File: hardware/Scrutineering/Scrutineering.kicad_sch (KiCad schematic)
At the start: 17 parts, among them J1 Conn_01x04, J10 Conn_01x03, J11 Conn_01x02, J12 Conn_01x01, J13 Conn_01x01, J2 Conn_01x04, J3 Conn_01x01, J4 Conn_01x01, J5 Conn_01x03, J6 Conn_01x04, J7 Conn_01x04, J8 Conn_01x01, J9 Conn_01x01, SW1 SW_SPDT_TEMP1, SW2 SW_SPDT_TEMP2, SW3 SW_SPDT_VOLT1, SW4 SW_SPDT_VOLT2

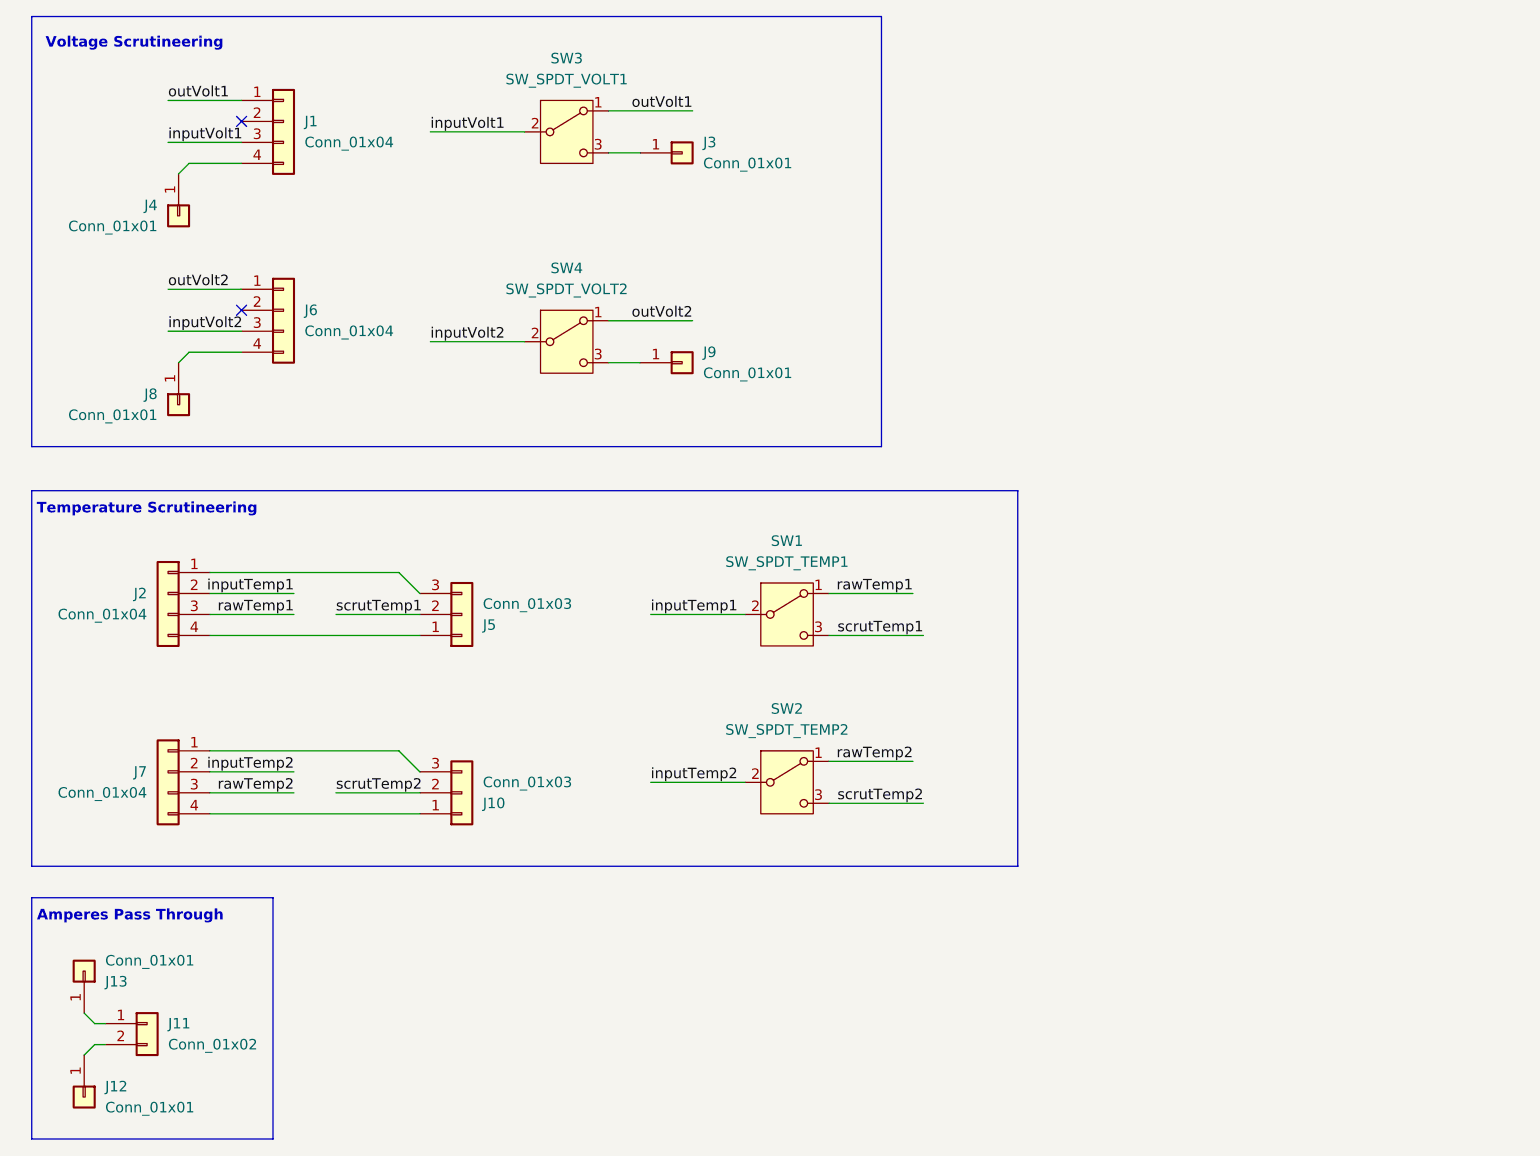
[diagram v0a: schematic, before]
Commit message: schematic with graphics/mounting
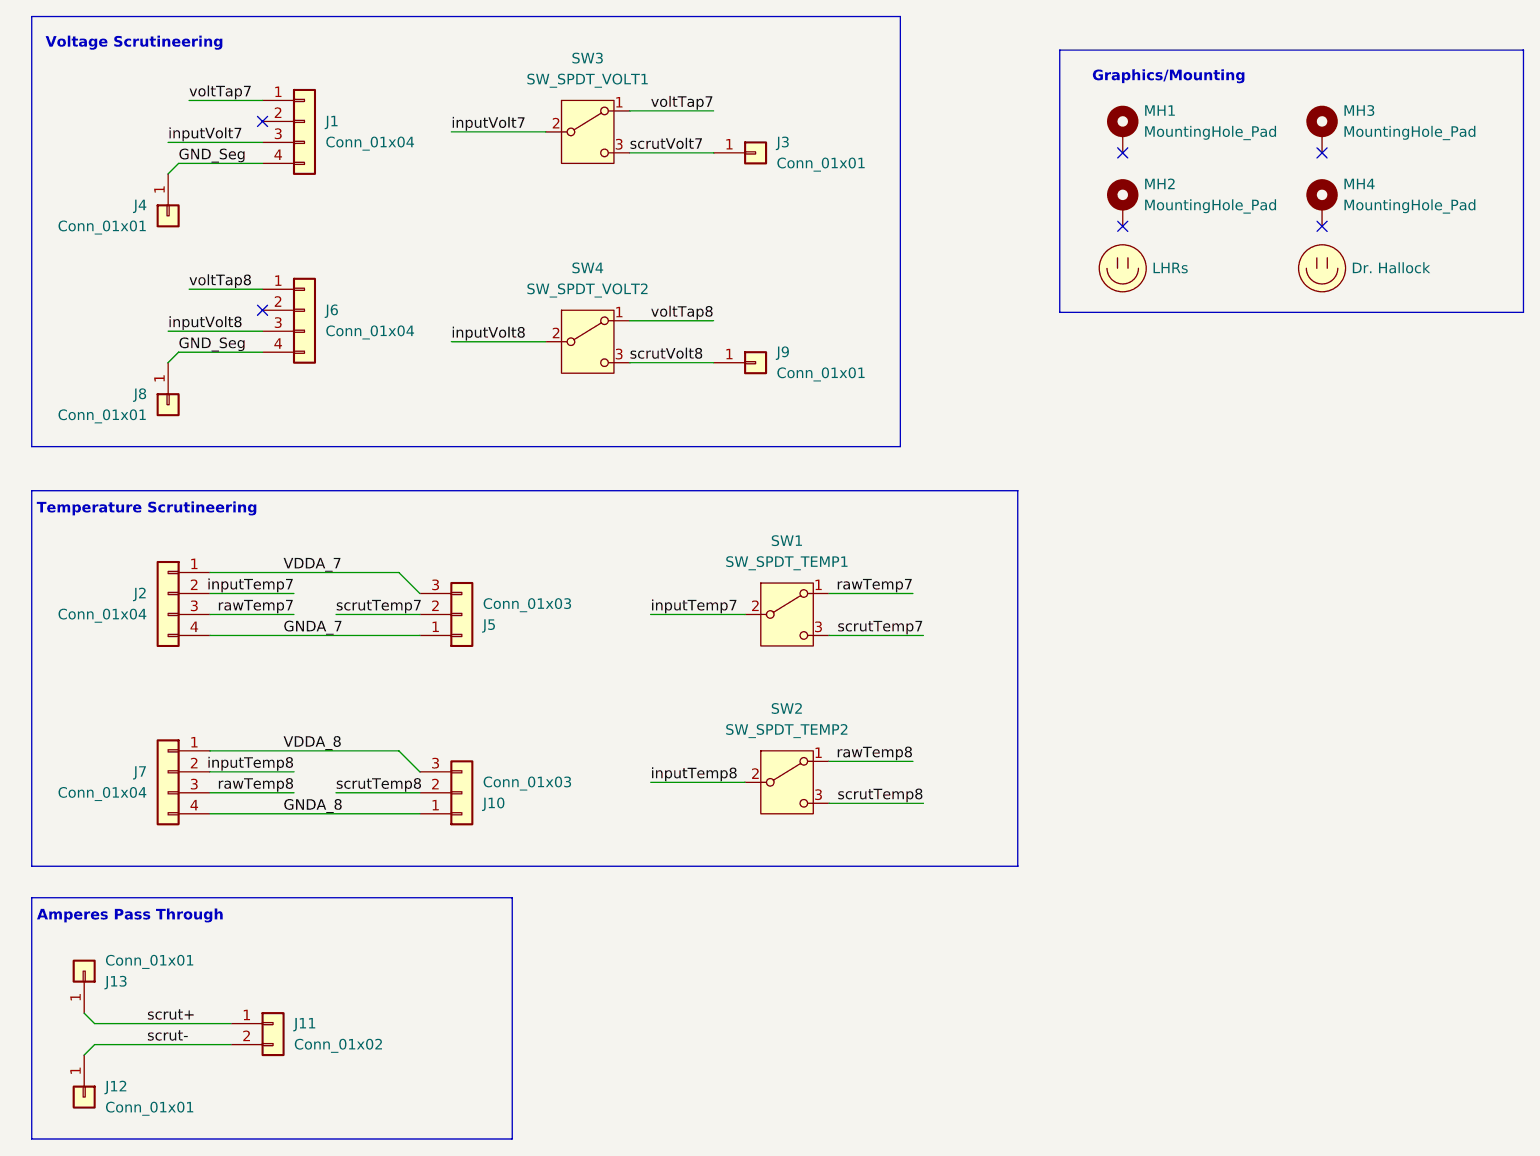
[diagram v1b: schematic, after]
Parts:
- added LOGO1: Dr. Hallock, UTSVT_Logos:Hallock_Image_Small, symbol utsvt_misc:Logo_Placeholder
- added LOGO2: LHRs, UTSVT_Logos:LHRs_LOGO, symbol utsvt_misc:Logo_Placeholder
- added MH1, MH2, MH3, MH4: MountingHole_Pad, MountingHole:MountingHole_3.2mm_M3_Pad_TopBottom, symbol Mechanical:MountingHole_Pad
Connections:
- net GND_Seg: now reaches J1.4 (Pin_4), J4.1 (Pin_1)
- net GND_Seg: now also J6.4 (Pin_4), J8.1 (Pin_1)
- net scrut+: now reaches J11.1 (Pin_1), J13.1 (Pin_1)
- net scrut-: now reaches J11.2 (Pin_2), J12.1 (Pin_1)
- net scrutVolt7: now reaches J3.1 (Pin_1), SW3.3 (C)
- net GNDA_7: now reaches J2.4 (Pin_4), J5.1 (Pin_1)
- net VDDA_7: now reaches J2.1 (Pin_1), J5.3 (Pin_3)
- net GNDA_8: now reaches J10.1 (Pin_1), J7.4 (Pin_4)
- net VDDA_8: now reaches J10.3 (Pin_3), J7.1 (Pin_1)
- net scrutVolt8: now reaches J9.1 (Pin_1), SW4.3 (C)
- net inputTemp1 renamed inputTemp7
- net inputTemp2 renamed inputTemp8
- net inputVolt1 renamed inputVolt7
- net inputVolt2 renamed inputVolt8
- net outVolt1 renamed voltTap7
- net outVolt2 renamed voltTap8
- net rawTemp1 renamed rawTemp7
- net rawTemp2 renamed rawTemp8
- net scrutTemp1 renamed scrutTemp7
- net scrutTemp2 renamed scrutTemp8
- no-connect marks 2 -> 6
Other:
- note added: "Graphics/Mounting"
- moved on the sheet: J1, J11, J3, J4, J6, J8, J9, SW3, SW4

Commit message: graphics stuff
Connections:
- net GND_Seg renamed GND_Seg7
- net GND_Seg7: no longer J6.4 (Pin_4), J8.1 (Pin_1)
- new net GND_Seg8: J6.4 (Pin_4), J8.1 (Pin_1)
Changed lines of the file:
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@@
 		)
 	)
-	(label "GND_Seg"
+	(label "GND_Seg7"
 		(at 44.45 45.72 0)
 		(effects
@@
 		)
 	)
-	(label "GND_Seg"
+	(label "GND_Seg8"
 		(at 44.45 68.58 0)
 		(effects

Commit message: BOM and gerber (still need to find jack P/N)
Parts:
- added J14: Conn_01x02, UTSVT_Connectors:105313-2102, symbol Connector_Generic:Conn_01x02
- renumbered J12 to J10, J5 to J11, J10 to J12, J11 to J13, J6 to J2, J2 to J3, J7 to J4, J4 to J5, J8 to J6, J3 to J7, J9 to J8, J13 to J9, SW3 to SW1, SW4 to SW2, SW1 to SW3, SW2 to SW4
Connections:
- net GNDA_7: now also J11.3 (Pin_3), J3.1 (Pin_1); no longer J11.1 (Pin_1), J3.4 (Pin_4)
- net GNDA_8: now also J12.3 (Pin_3), J4.1 (Pin_1); no longer J12.1 (Pin_1), J4.4 (Pin_4)
- net GND_Seg7: now also J1.1 (Pin_1); no longer J1.4 (Pin_4)
- net GND_Seg8: now also J2.1 (Pin_1); no longer J2.4 (Pin_4)
- net VDDA_7: now also J11.1 (Pin_1), J3.4 (Pin_4); no longer J11.3 (Pin_3), J3.1 (Pin_1)
- net VDDA_8: now also J12.1 (Pin_1), J4.4 (Pin_4); no longer J12.3 (Pin_3), J4.1 (Pin_1)
- net inputVolt7: now also J1.2 (Pin_2); no longer J1.3 (Pin_3)
- net inputVolt8: now also J2.2 (Pin_2); no longer J2.3 (Pin_3)
- net scrut+: now also J14.2 (Pin_2)
- net scrut-: now also J14.1 (Pin_1)
- net voltTap7: now also J1.4 (Pin_4); no longer J1.1 (Pin_1)
- net voltTap8: now also J2.4 (Pin_4); no longer J2.1 (Pin_1)
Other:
- moved on the sheet: J1, J2, J3, J4, J5, J6

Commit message: final
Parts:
- J10, J5, J6, J7, J8, J9: P/N (none) -> 105-2210-201
- TEMP1: renamed from SW3; value SW_SPDT_TEMP1 -> SW_SPDT; P/N (none) -> OS102011MS2Q
- TEMP2: renamed from SW4; value SW_SPDT_TEMP2 -> SW_SPDT; P/N (none) -> OS102011MS2Q
- VOLT1: renamed from SW1; value SW_SPDT_VOLT1 -> SW_SPDT; P/N (none) -> OS102011MS2Q
- VOLT2: renamed from SW2; value SW_SPDT_VOLT2 -> SW_SPDT; P/N (none) -> OS102011MS2Q
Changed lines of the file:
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@@
+			)
+		)
+		(property "P/N" "105-2210-201"
+			(at 114.3 44.45 0)
+			(effects
+				(font
+					(size 1.27 1.27)
+				)
+				(hide yes)
 			)
 		)
@@
 			)
 		)
+		(property "P/N" "105-2210-201"
+			(at 33.02 158.75 90)
+			(effects
+				(font
+					(size 1.27 1.27)
+				)
+				(hide yes)
+			)
+		)
 		(pin "1"
 		)
@@
 			)
 		)
+		(property "P/N" "105-2210-201"
+			(at 59.69 52.07 90)
+			(effects
+				(font
+					(size 1.27 1.27)
+				)
+				(hide yes)
+			)
+		)
 		(pin "1"
 		)
@@
 		(dnp no)
 		(fields_autoplaced yes)
-		(property "Reference" "SW1"
+		(property "Reference" "VOLT1"
 			(at 93.98 33.02 0)
 			(effects
@@
 			)
 		)
-		(property "Value" "SW_SPDT_VOLT1"
+		(property "Value" "SW_SPDT"
 			(at 93.98 35.56 0)
 			(effects
@@
 			)
 		)
+		(property "P/N" "OS102011MS2Q"
+			(at 93.98 41.91 0)
+			(effects
+				(font
+					(size 1.27 1.27)
+				)
+				(hide yes)
+			)
+		)
 		(pin "1"
 		)
@@
 			(project "Scrutineering"
 				(path "/1bd27d0d-b5e6-43a9-9122-71eb8007bcd4"
-					(reference "SW1")
+					(reference "VOLT1")
 					(unit 1)
 				)
@@
 			)
 		)
+		(property "P/N" "105-2210-201"
+			(at 33.02 143.51 90)
+			(effects
+				(font
+					(size 1.27 1.27)
+				)
+				(hide yes)
+			)
+		)
 		(pin "1"
 		)
@@
 		(dnp no)
 		(fields_autoplaced yes)
-		(property "Reference" "SW2"
+		(property "Reference" "VOLT2"
 			(at 93.98 58.42 0)
 			(effects
@@
 			)
 		)
-		(property "Value" "SW_SPDT_VOLT2"
+		(property "Value" "SW_SPDT"
 			(at 93.98 60.96 0)
 			(effects
@@
 			)
 		)
+		(property "P/N" "OS102011MS2Q"
+			(at 93.98 67.31 0)
+			(effects
+				(font
+					(size 1.27 1.27)
+				)
+				(hide yes)
+			)
+		)
 		(pin "1"
 		)
@@
 			(project "Scrutineering"
 				(path "/1bd27d0d-b5e6-43a9-9122-71eb8007bcd4"
-					(reference "SW2")
+					(reference "VOLT2")
 					(unit 1)
 				)
@@
 			)
 		)
+		(property "P/N" "105-2210-201"
+			(at 59.69 74.93 90)
+			(effects
+				(font
+					(size 1.27 1.27)
+				)
+				(hide yes)
+			)
+		)
 		(pin "1"
 		)
@@
 			)
 		)
+		(property "P/N" "105-2210-201"
+			(at 114.3 69.85 0)
+			(effects
+				(font
+					(size 1.27 1.27)
+				)
+				(hide yes)
+			)
+		)
 		(pin "1"
 		)
@@
 		(dnp no)
 		(fields_autoplaced yes)
-		(property "Reference" "SW3"
+		(property "Reference" "TEMP1"
 			(at 118.11 91.44 0)
 			(effects
@@
 			)
 		)
-		(property "Value" "SW_SPDT_TEMP1"
+		(property "Value" "SW_SPDT"
 			(at 118.11 93.98 0)
 			(effects
@@
 			)
 		)
+		(property "P/N" "OS102011MS2Q"
+			(at 118.11 100.33 0)
+			(effects
+				(font
+					(size 1.27 1.27)
+				)
+				(hide yes)
+			)
+		)
 		(pin "1"
 		)
@@
 			(project "Scrutineering"
 				(path "/1bd27d0d-b5e6-43a9-9122-71eb8007bcd4"
-					(reference "SW3")
+					(reference "TEMP1")
 					(unit 1)
 				)
@@
 		(dnp no)
 		(fields_autoplaced yes)
-		(property "Reference" "SW4"
+		(property "Reference" "TEMP2"
 			(at 118.11 111.76 0)
 			(effects
@@
 			)
 		)
-		(property "Value" "SW_SPDT_TEMP2"
+		(property "Value" "SW_SPDT"
 			(at 118.11 114.3 0)
 			(effects
@@
 			)
 		)
+		(property "P/N" "OS102011MS2Q"
+			(at 118.11 120.65 0)
+			(effects
+				(font
+					(size 1.27 1.27)
+				)
+				(hide yes)
+			)
+		)
 		(pin "1"
 		)
@@
 			(project ""
 				(path "/1bd27d0d-b5e6-43a9-9122-71eb8007bcd4"
-					(reference "SW4")
-					(unit 1)
-				)
+					(reference "TEMP2")
+					(unit 1)
+				)

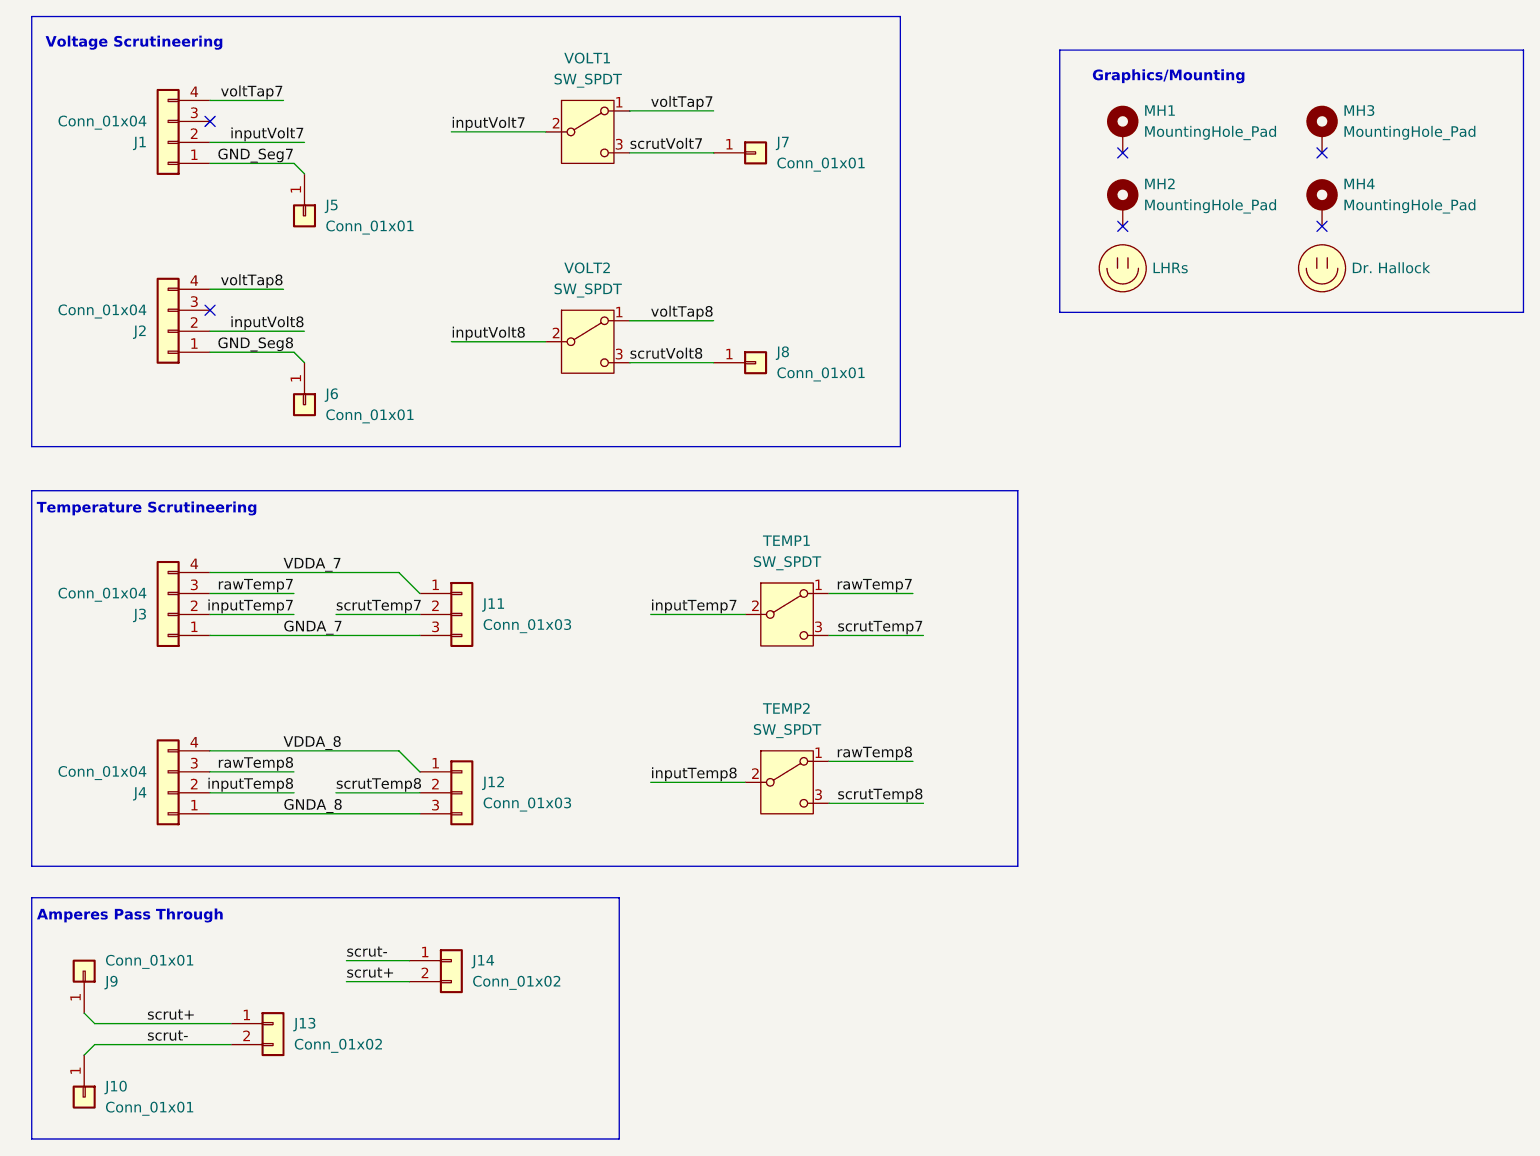
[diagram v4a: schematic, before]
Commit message: BOM and gerber with changed connector
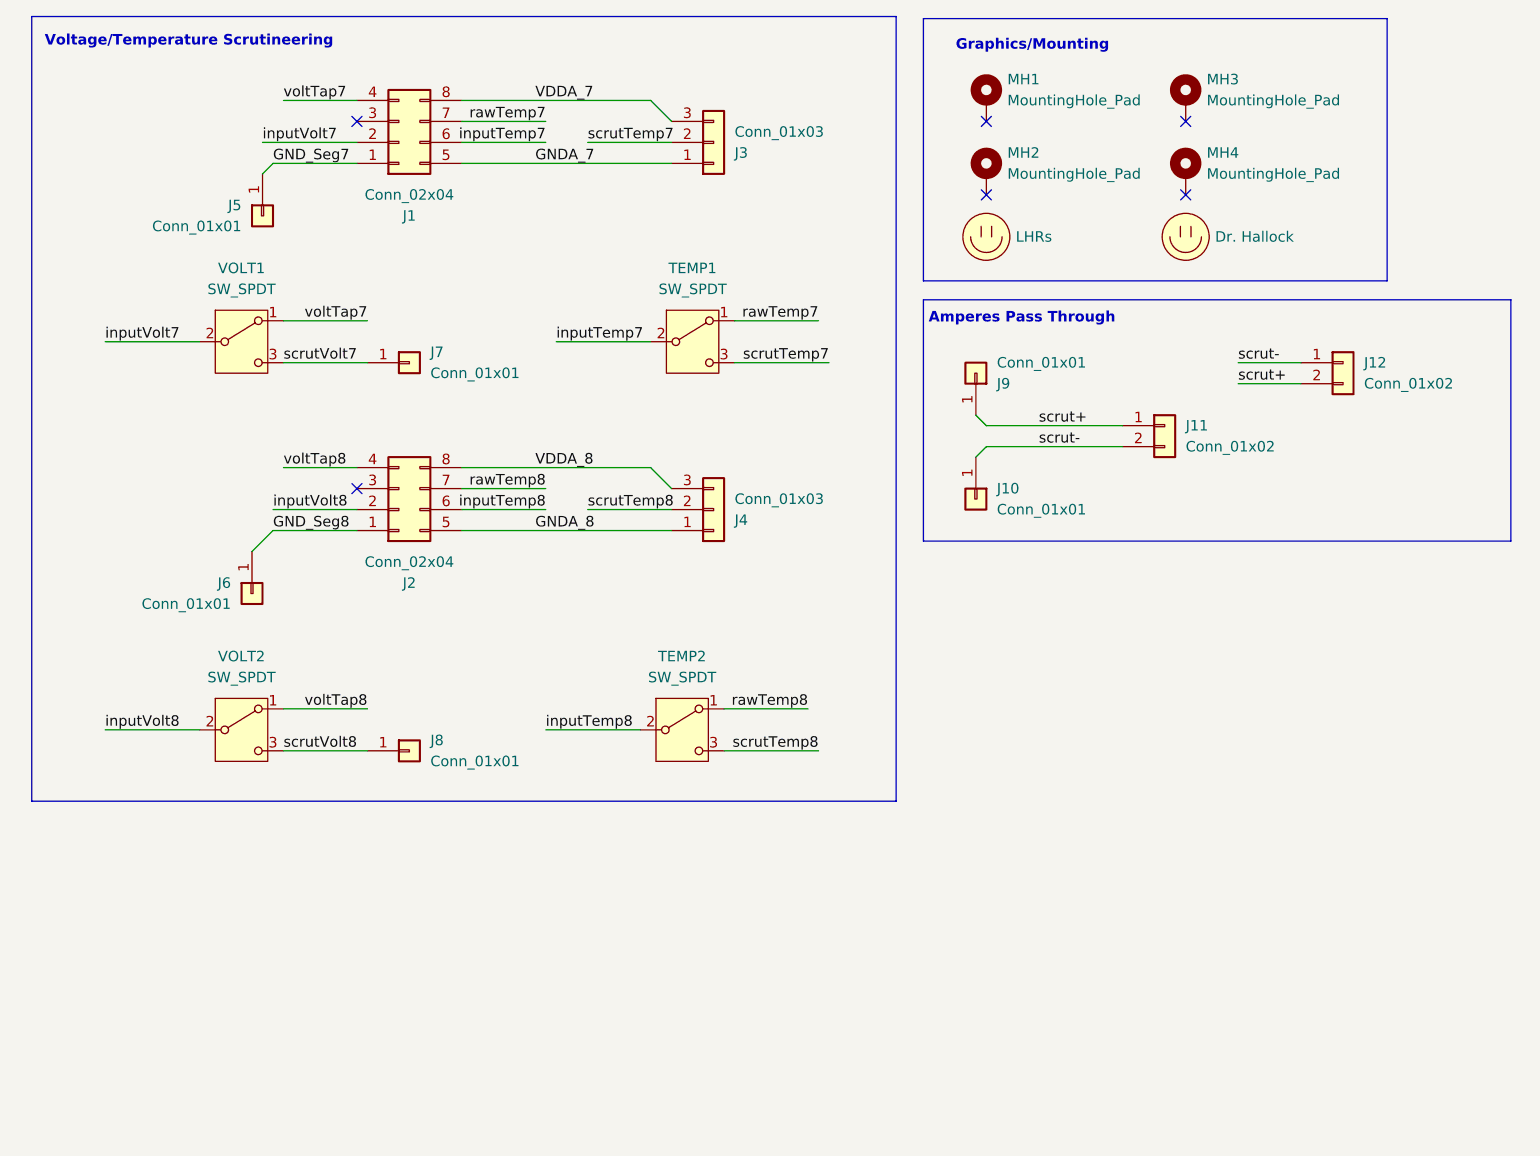
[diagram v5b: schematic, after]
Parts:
- removed J1, J2, J3, J4: Conn_01x04, VoltTemp:1053132104, symbol Connector_Generic:Conn_01x04
- removed J11, J12: Conn_01x03, VoltTemp:1053131103, symbol Connector_Generic:Conn_01x03
- added J1, J2: Conn_02x04, Scrutineering:nanofit_02x04, symbol Connector_Generic:Conn_02x04_Top_Bottom
- added J3, J4: Conn_01x03, VoltTemp:1053131103, symbol Connector_Generic:Conn_01x03
- renumbered J13 to J11, J14 to J12
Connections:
- net GNDA_7: now also J1.5 (Pin_5), J3.1 (Pin_1)
- net GNDA_8: now also J2.5 (Pin_5), J4.1 (Pin_1)
- net GND_Seg7: now also J1.1 (Pin_1)
- net GND_Seg8: now also J2.1 (Pin_1)
- net VDDA_7: now also J1.8 (Pin_8), J3.3 (Pin_3)
- net VDDA_8: now also J2.8 (Pin_8), J4.3 (Pin_3)
- net inputTemp7: now also J1.6 (Pin_6)
- net inputTemp8: now also J2.6 (Pin_6)
- net inputVolt7: now also J1.2 (Pin_2)
- net inputVolt8: now also J2.2 (Pin_2)
- net rawTemp7: now also J1.7 (Pin_7)
- net rawTemp8: now also J2.7 (Pin_7)
- net scrutTemp7: now also J3.2 (Pin_2)
- net scrutTemp8: now also J4.2 (Pin_2)
- net voltTap7: now also J1.4 (Pin_4)
- net voltTap8: now also J2.4 (Pin_4)
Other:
- note added: "Voltage/Temperature Scrutineering"
- note removed: "Temperature Scrutineering"
- note removed: "Voltage Scrutineering"
- moved on the sheet: J10, J11, J12, J7, J8, J9, MH1, MH2, MH3, MH4, TEMP1, TEMP2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
